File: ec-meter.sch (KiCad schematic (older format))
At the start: 24 parts, among them U1 LM324

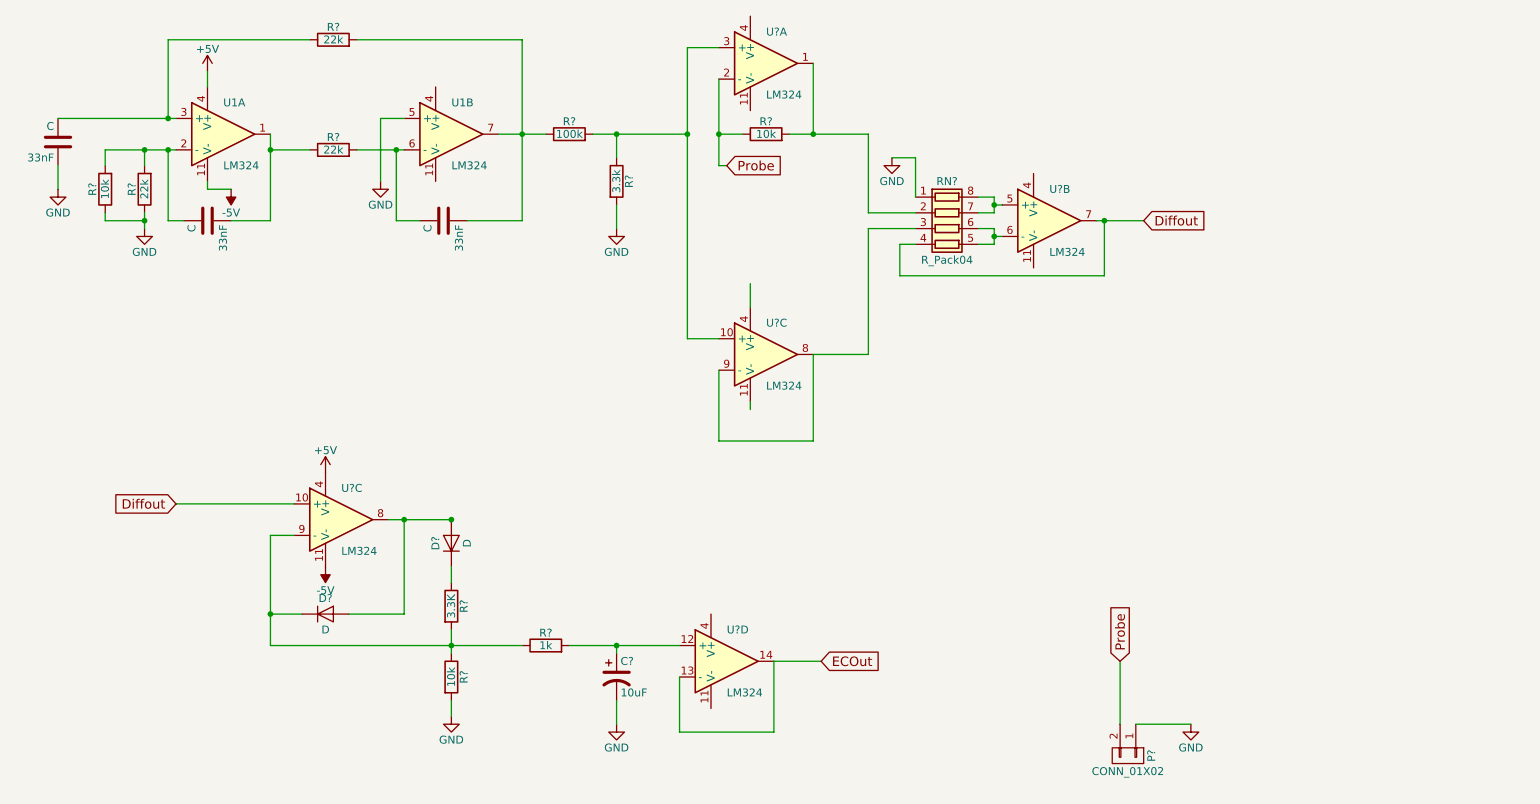
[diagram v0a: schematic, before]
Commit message: Got schematic to pass DRC
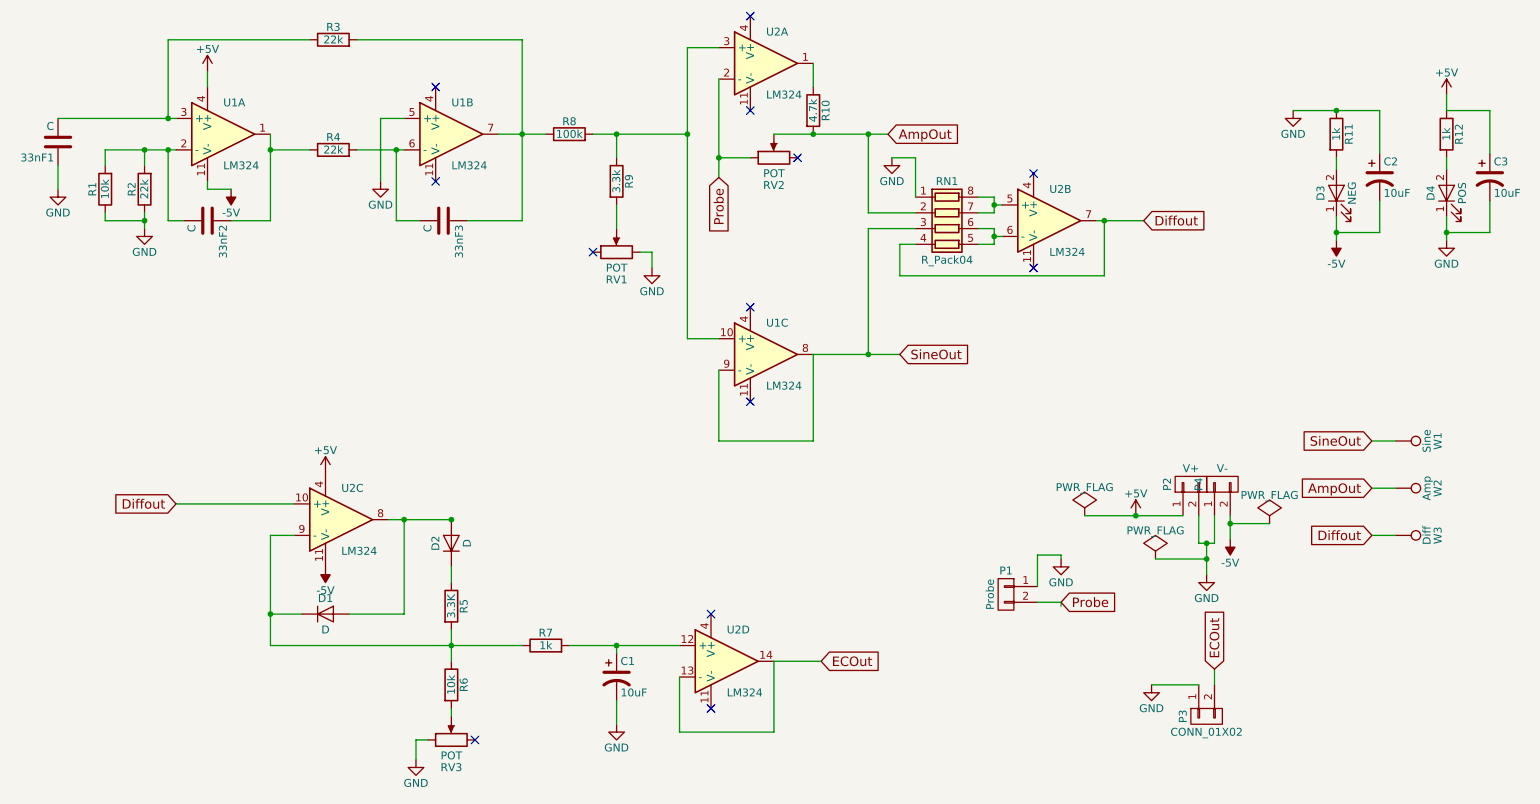
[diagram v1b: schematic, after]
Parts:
- added C2, C3: 10uF, symbol CP1
- added D3: NEG, symbol LED
- added D4: POS, symbol LED
- added P2: V+, symbol CONN_01X02
- added P3: CONN_01X02, symbol CONN_01X02
- added P4: V-, symbol CONN_01X02
- added R11, R12: 1k, symbol R
- added RV1, RV2, RV3: POT, symbol POT
- added W1: Sine, symbol TEST_1P
- added W2: Amp, symbol TEST_1P
- added W3: Diff, symbol TEST_1P
- P1: renamed from P?; value CONN_01X02 -> Probe
- R10: renamed from R?; value 10k -> 4.7k
- gave numbers to parts that had none: 15
- renumbered 33nF to 33nF1, 33nF to 33nF2, 33nF to 33nF3
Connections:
- net +5V: now also C3.1, P2.1 (P1), R12.1
- net -5V: now also C2.2, D3.1 (K), P4.2 (P2)
- net Diffout: now also W3.1
- net ECOut: now also P3.2 (P2)
- net GND: now also C2.1, C3.2, D4.1 (K), P2.2 (P2), P3.1 (P1), P4.1 (P1), R11.1, RV1.3, RV3.1; no longer R6.2, R9.2
- net Probe: now also RV2.1; no longer R10.1
- net AmpOut: now reaches R10.2, RN1.2 (R2.1)
- net AmpOut: now also RV2.2, W2.1; no longer U2.1
- net SineOut: now reaches RN1.3 (R3.1), U1.8, U1.9 (-)
- net SineOut: now also W1.1
- new net: R9.2, RV1.2
- new net: R10.1, U2.1
- new net: R6.2, RV3.2
- new net: D3.2 (A), R11.2
- new net: D4.2 (A), R12.2
- no-connect marks 0 -> 13
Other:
- moved on the sheet: P1, R10, R6

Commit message: Mapped componets, fixed some references
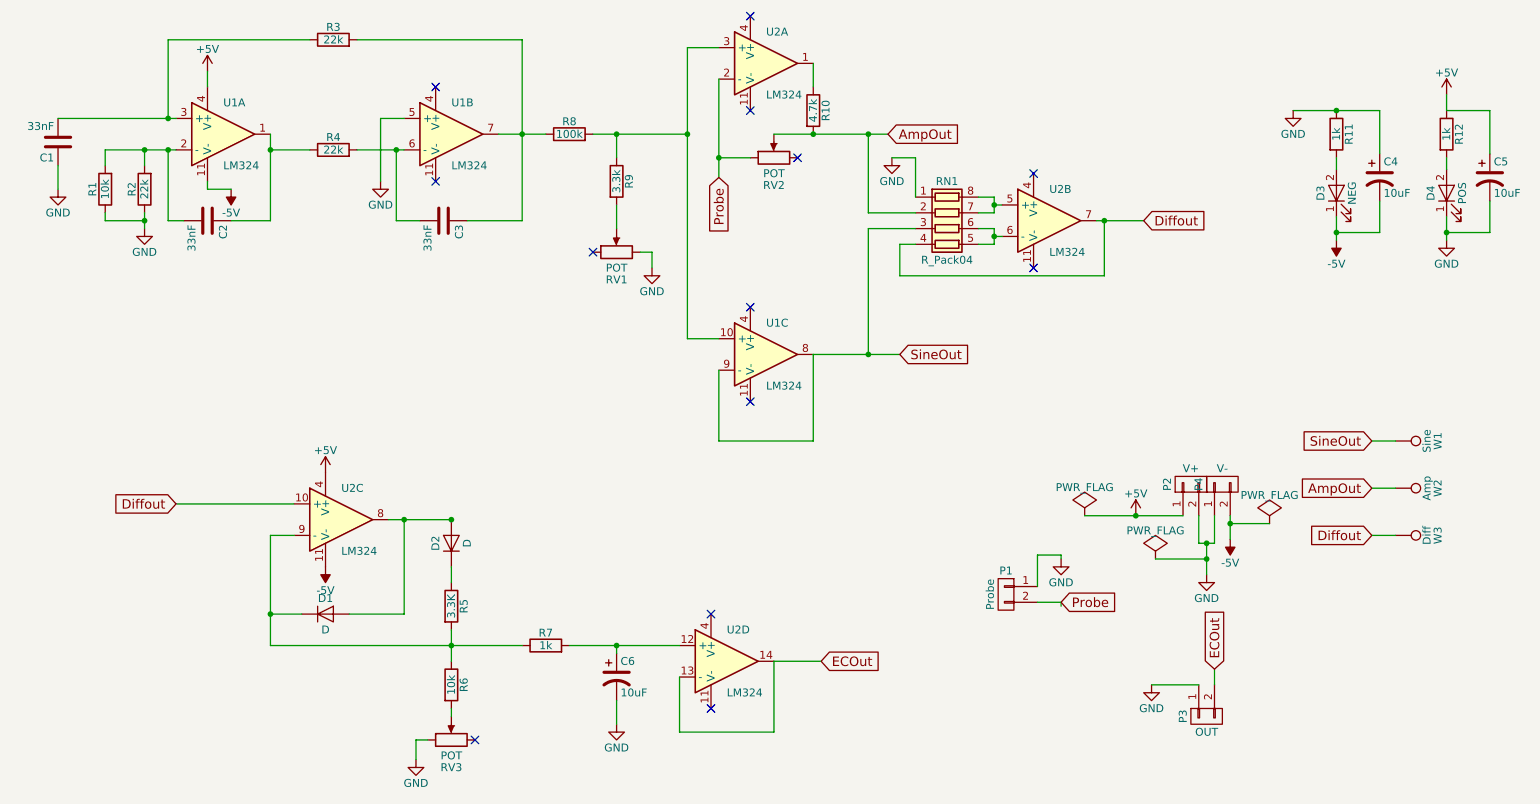
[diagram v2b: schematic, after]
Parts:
- C1: renamed from 33nF1; value C -> 33nF; footprint (none) -> visgence_parts:SM1206POL_VIS
- C2: renamed from 33nF2; value C -> 33nF; footprint (none) -> visgence_parts:SM1206POL_VIS
- C3: renamed from 33nF3; value C -> 33nF; footprint (none) -> visgence_parts:SM1206POL_VIS
- C4: renamed from C2; footprint (none) -> visgence_parts:SM1206POL_VIS
- C6: renamed from C1; footprint (none) -> visgence_parts:SM1206POL_VIS
- P3: value CONN_01X02 -> OUT
- R1, R10, R11, R12, R2, R3, R4, R5, R6, R7, R8, R9: footprint (none) -> visgence_parts:SM1206_VIS
- RN1: footprint (none) -> visgence_parts:RESARRAY-0612
- RV1, RV2, RV3: footprint (none) -> visgence_parts:Var_resistor
- U1, U2: footprint (none) -> SMD_Packages:SOIC-14_N
- W1, W2, W3: footprint (none) -> Measurement_Points:Measurement_Point_Square-TH_Small
- renumbered C3 to C5
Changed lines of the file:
@@
 F 0 "U1" H 2100 2050 50  0000 L CNN
 F 1 "LM324" H 2100 1650 50  0000 L CNN
-F 2 "" H 2050 1950 50  0000 C CNN
+F 2 "SMD_Packages:SOIC-14_N" H 2050 1950 50  0001 C CNN
 F 3 "" H 2150 2050 50  0000 C CNN
 	1    2100 1850
@@
 F 0 "U1" H 3550 2050 50  0000 L CNN
 F 1 "LM324" H 3550 1650 50  0000 L CNN
-F 2 "" H 3500 1950 50  0000 C CNN
+F 2 "SMD_Packages:SOIC-14_N" H 3500 1950 50  0001 C CNN
 F 3 "" H 3600 2050 50  0000 C CNN
 	2    3550 1850
@@
 F 0 "R4" V 2880 1950 50  0000 C CNN
 F 1 "22k" V 2800 1950 50  0000 C CNN
-F 2 "" V 2730 1950 50  0000 C CNN
+F 2 "visgence_parts:SM1206_VIS" V 2730 1950 50  0001 C CNN
 F 3 "" H 2800 1950 50  0000 C CNN
 	1    2800 1950
@@
 F 0 "R2" V 1680 2200 50  0000 C CNN
 F 1 "22k" V 1600 2200 50  0000 C CNN
-F 2 "" V 1530 2200 50  0000 C CNN
+F 2 "visgence_parts:SM1206_VIS" V 1530 2200 50  0001 C CNN
 F 3 "" H 1600 2200 50  0000 C CNN
 	1    1600 2200
@@
 F 0 "R1" V 1430 2200 50  0000 C CNN
 F 1 "10k" V 1350 2200 50  0000 C CNN
-F 2 "" V 1280 2200 50  0000 C CNN
+F 2 "visgence_parts:SM1206_VIS" V 1280 2200 50  0001 C CNN
 F 3 "" H 1350 2200 50  0000 C CNN
 	1    1350 2200
@@
 Connection ~ 1600 2400
 $Comp
-L C 33nF2
+L C C2
 U 1 1 58825F83
 P 2000 2400
-F 0 "33nF2" H 2025 2500 50  0000 L CNN
-F 1 "C" H 2025 2300 50  0000 L CNN
-F 2 "" H 2038 2250 50  0000 C CNN
+F 0 "C2" H 2025 2500 50  0000 L CNN
+F 1 "33nF" H 2025 2300 50  0000 L CNN
+F 2 "visgence_parts:SM1206POL_VIS" H 2038 2250 50  0001 C CNN
 F 3 "" H 2000 2400 50  0000 C CNN
 	1    2000 2400
@@
 Connection ~ 1750 1950
 $Comp
-L C 33nF1
+L C C1
 U 1 1 5882608A
 P 1050 1900
-F 0 "33nF1" H 1075 2000 50  0000 L CNN
-F 1 "C" H 1075 1800 50  0000 L CNN
-F 2 "" H 1088 1750 50  0000 C CNN
+F 0 "C1" H 1075 2000 50  0000 L CNN
+F 1 "33nF" H 1075 1800 50  0000 L CNN
+F 2 "visgence_parts:SM1206POL_VIS" H 1088 1750 50  0001 C CNN
 F 3 "" H 1050 1900 50  0000 C CNN
 	1    1050 1900
@@
 F 0 "R3" V 2880 1250 50  0000 C CNN
 F 1 "22k" V 2800 1250 50  0000 C CNN
-F 2 "" V 2730 1250 50  0000 C CNN
+F 2 "visgence_parts:SM1206_VIS" V 2730 1250 50  0001 C CNN
 F 3 "" H 2800 1250 50  0000 C CNN
 	1    2800 1250
@@
 	4000 2400 4000 1250
 $Comp
-L C 33nF3
+L C C3
 U 1 1 58826293
 P 3500 2400
-F 0 "33nF3" H 3525 2500 50  0000 L CNN
-F 1 "C" H 3525 2300 50  0000 L CNN
-F 2 "" H 3538 2250 50  0000 C CNN
+F 0 "C3" H 3525 2500 50  0000 L CNN
+F 1 "33nF" H 3525 2300 50  0000 L CNN
+F 2 "visgence_parts:SM1206POL_VIS" H 3538 2250 50  0001 C CNN
 F 3 "" H 3500 2400 50  0000 C CNN
 	1    3500 2400
@@
 F 0 "R8" V 4380 1850 50  0000 C CNN
 F 1 "100k" V 4300 1850 50  0000 C CNN
-F 2 "" V 4230 1850 50  0000 C CNN
+F 2 "visgence_parts:SM1206_VIS" V 4230 1850 50  0001 C CNN
 F 3 "" H 4300 1850 50  0000 C CNN
 	1    4300 1850
@@
 F 0 "R9" V 4680 2150 50  0000 C CNN
 F 1 "3.3k" V 4600 2150 50  0000 C CNN
-F 2 "" V 4530 2150 50  0000 C CNN
+F 2 "visgence_parts:SM1206_VIS" V 4530 2150 50  0001 C CNN
 F 3 "" H 4600 2150 50  0000 C CNN
 	1    4600 2150
@@
 F 0 "U2" H 5550 1600 50  0000 L CNN
 F 1 "LM324" H 5550 1200 50  0000 L CNN
-F 2 "" H 5500 1500 50  0000 C CNN
+F 2 "SMD_Packages:SOIC-14_N" H 5500 1500 50  0001 C CNN
 F 3 "" H 5600 1600 50  0000 C CNN
 	1    5550 1400
@@
 F 0 "U2" H 7350 2600 50  0000 L CNN
 F 1 "LM324" H 7350 2200 50  0000 L CNN
-F 2 "" H 7300 2500 50  0000 C CNN
+F 2 "SMD_Packages:SOIC-14_N" H 7300 2500 50  0001 C CNN
 F 3 "" H 7400 2600 50  0000 C CNN
 	2    7350 2400
@@
 F 0 "U2" H 2850 4500 50  0000 L CNN
 F 1 "LM324" H 2850 4100 50  0000 L CNN
-F 2 "" H 2800 4400 50  0000 C CNN
+F 2 "SMD_Packages:SOIC-14_N" H 2800 4400 50  0001 C CNN
 F 3 "" H 2900 4500 50  0000 C CNN
 	3    2850 4300
@@
 F 0 "U2" H 5300 5400 50  0000 L CNN
 F 1 "LM324" H 5300 5000 50  0000 L CNN
-F 2 "" H 5250 5300 50  0000 C CNN
+F 2 "SMD_Packages:SOIC-14_N" H 5250 5300 50  0001 C CNN
 F 3 "" H 5350 5400 50  0000 C CNN
 	4    5300 5200
@@
 F 0 "R10" V 5930 1700 50  0000 C CNN
 F 1 "4.7k" V 5850 1700 50  0000 C CNN
-F 2 "" V 5780 1700 50  0000 C CNN
+F 2 "visgence_parts:SM1206_VIS" V 5780 1700 50  0001 C CNN
 F 3 "" H 5850 1700 50  0000 C CNN
 	1    5850 1700
@@
 F 0 "P1" H 7075 4925 50  0000 C CNN
 F 1 "Probe" V 7175 4775 50  0000 C CNN
-F 2 "" H 7075 4775 50  0000 C CNN
+F 2 "" H 7075 4775 50  0001 C CNN
 F 3 "" H 7075 4775 50  0000 C CNN
 	1    7075 4775
@@
 F 0 "RN1" V 6400 2450 50  0000 C CNN
 F 1 "R_Pack04" V 6900 2450 50  0000 C CNN
-F 2 "" V 6975 2450 50  0001 C CNN
+F 2 "visgence_parts:RESARRAY-0612" V 6975 2450 50  0001 C CNN
 F 3 "" H 6700 2450 50  0000 C CNN
 	1    6700 2450
@@
 F 0 "D1" H 2750 5000 50  0000 C CNN
 F 1 "D" H 2750 4800 50  0000 C CNN
-F 2 "" H 2750 4900 50  0000 C CNN
+F 2 "" H 2750 4900 50  0001 C CNN
 F 3 "" H 2750 4900 50  0000 C CNN
 	1    2750 4900
@@
 F 0 "D2" H 3550 4550 50  0000 C CNN
 F 1 "D" H 3550 4350 50  0000 C CNN
-F 2 "" H 3550 4450 50  0000 C CNN
+F 2 "" H 3550 4450 50  0001 C CNN
 F 3 "" H 3550 4450 50  0000 C CNN
 	1    3550 4450
@@
 F 0 "R5" V 3630 4850 50  0000 C CNN
 F 1 "3.3K" V 3550 4850 50  0000 C CNN
-F 2 "" V 3480 4850 50  0000 C CNN
+F 2 "visgence_parts:SM1206_VIS" V 3480 4850 50  0001 C CNN
 F 3 "" H 3550 4850 50  0000 C CNN
 	1    3550 4850
@@
 F 0 "R7" V 4230 5100 50  0000 C CNN
 F 1 "1k" V 4150 5100 50  0000 C CNN
-F 2 "" V 4080 5100 50  0000 C CNN
+F 2 "visgence_parts:SM1206_VIS" V 4080 5100 50  0001 C CNN
 F 3 "" H 4150 5100 50  0000 C CNN
 	1    4150 5100
@@
 Connection ~ 3550 5100
 $Comp
-L CP1 C1
+L CP1 C6
 U 1 1 5882F85D
 P 4600 5300
-F 0 "C1" H 4625 5400 50  0000 L CNN
+F 0 "C6" H 4625 5400 50  0000 L CNN
 F 1 "10uF" H 4625 5200 50  0000 L CNN
-F 2 "" H 4600 5300 50  0000 C CNN
+F 2 "visgence_parts:SM1206POL_VIS" H 4600 5300 50  0001 C CNN
 F 3 "" H 4600 5300 50  0000 C CNN
 	1    4600 5300
@@
 F 0 "U1" H 5550 3450 50  0000 L CNN
 F 1 "LM324" H 5550 3050 50  0000 L CNN
-F 2 "" H 5500 3350 50  0000 C CNN
+F 2 "SMD_Packages:SOIC-14_N" H 5500 3350 50  0001 C CNN
 F 3 "" H 5600 3450 50  0000 C CNN
 	3    5550 3250
@@
 F 0 "P2" H 8250 4225 50  0000 C CNN
 F 1 "V+" V 8350 4075 50  0000 C CNN
-F 2 "" H 8250 4075 50  0000 C CNN
+F 2 "" H 8250 4075 50  0001 C CNN
 F 3 "" H 8250 4075 50  0000 C CNN
 	1    8250 4075
@@
 F 0 "P4" H 8450 4225 50  0000 C CNN
 F 1 "V-" V 8550 4075 50  0000 C CNN
-F 2 "" H 8450 4075 50  0000 C CNN
+F 2 "" H 8450 4075 50  0001 C CNN
 F 3 "" H 8450 4075 50  0000 C CNN
 	1    8450 4075
@@
 P 8350 5550
 F 0 "P3" H 8350 5700 50  0000 C CNN
-F 1 "CONN_01X02" V 8450 5550 50  0000 C CNN
-F 2 "" H 8350 5550 50  0000 C CNN
+F 1 "OUT" V 8450 5550 50  0000 C CNN
+F 2 "" H 8350 5550 50  0001 C CNN
 F 3 "" H 8350 5550 50  0000 C CNN
 	1    8350 5550
@@
 F 0 "RV2" V 5425 2000 50  0000 C CNN
 F 1 "POT" V 5500 2000 50  0000 C CNN
-F 2 "" H 5600 2000 50  0000 C CNN
+F 2 "visgence_parts:Var_resistor" H 5600 2000 50  0001 C CNN
 F 3 "" H 5600 2000 50  0000 C CNN
 	1    5600 2000
@@
 F 0 "RV3" V 3375 5700 50  0000 C CNN
 F 1 "POT" V 3450 5700 50  0000 C CNN
-F 2 "" H 3550 5700 50  0000 C CNN
+F 2 "visgence_parts:Var_resistor" H 3550 5700 50  0001 C CNN
 F 3 "" H 3550 5700 50  0000 C CNN
 	1    3550 5700
@@
 F 0 "R6" V 3630 5350 50  0000 C CNN
 F 1 "10k" V 3550 5350 50  0000 C CNN
-F 2 "" V 3480 5350 50  0000 C CNN
+F 2 "visgence_parts:SM1206_VIS" V 3480 5350 50  0001 C CNN
 F 3 "" H 3550 5350 50  0000 C CNN
 	1    3550 5350
@@
 F 0 "RV1" V 4425 2600 50  0000 C CNN
 F 1 "POT" V 4500 2600 50  0000 C CNN
-F 2 "" H 4600 2600 50  0000 C CNN
+F 2 "visgence_parts:Var_resistor" H 4600 2600 50  0001 C CNN
 F 3 "" H 4600 2600 50  0000 C CNN
 	1    4600 2600
@@
 F 0 "R11" V 9255 1850 50  0000 C CNN
 F 1 "1k" V 9175 1850 50  0000 C CNN
-F 2 "" V 9105 1850 50  0000 C CNN
+F 2 "visgence_parts:SM1206_VIS" V 9105 1850 50  0001 C CNN
 F 3 "" H 9175 1850 50  0000 C CNN
 	1    9175 1850
@@
 F 0 "D3" H 9175 2325 50  0000 C CNN
 F 1 "NEG" H 9175 2125 50  0000 C CNN
-F 2 "" H 9175 2225 50  0000 C CNN
+F 2 "" H 9175 2225 50  0001 C CNN
 F 3 "" H 9175 2225 50  0000 C CNN
 	1    9175 2225
@@
 Connection ~ 9175 2475
 $Comp
-L CP1 C2
+L CP1 C4
 U 1 1 5886CB8B
 P 9450 2125
-F 0 "C2" H 9475 2225 50  0000 L CNN
+F 0 "C4" H 9475 2225 50  0000 L CNN
 F 1 "10uF" H 9475 2025 50  0000 L CNN
-F 2 "" H 9450 2125 50  0000 C CNN
+F 2 "visgence_parts:SM1206POL_VIS" H 9450 2125 50  0001 C CNN
 F 3 "" H 9450 2125 50  0000 C CNN
 	1    9450 2125
@@
 F 0 "R12" V 9955 1850 50  0000 C CNN
 F 1 "1k" V 9875 1850 50  0000 C CNN
-F 2 "" V 9805 1850 50  0000 C CNN
+F 2 "visgence_parts:SM1206_VIS" V 9805 1850 50  0001 C CNN
 F 3 "" H 9875 1850 50  0000 C CNN
 	1    9875 1850
@@
 F 0 "D4" H 9875 2325 50  0000 C CNN
 F 1 "POS" H 9875 2125 50  0000 C CNN
-F 2 "" H 9875 2225 50  0000 C CNN
+F 2 "" H 9875 2225 50  0001 C CNN
 F 3 "" H 9875 2225 50  0000 C CNN
 	1    9875 2225
@@
 Connection ~ 9875 2475
 $Comp
-L CP1 C3
+L CP1 C5
 U 1 1 5886D1CB
 P 10150 2125
-F 0 "C3" H 10175 2225 50  0000 L CNN
+F 0 "C5" H 10175 2225 50  0000 L CNN
 F 1 "10uF" H 10175 2025 50  0000 L CNN
-F 2 "" H 10150 2125 50  0000 C CNN
+F 2 "" H 10150 2125 50  0001 C CNN
 F 3 "" H 10150 2125 50  0000 C CNN
 	1    10150 2125
@@
 F 0 "W1" H 9550 4070 50  0000 C CNN
 F 1 "Sine" H 9550 4000 50  0000 C CNN
-F 2 "" H 9750 3800 50  0000 C CNN
+F 2 "Measurement_Points:Measurement_Point_Square-TH_Small" H 9750 3800 50  0001 C CNN
 F 3 "" H 9750 3800 50  0000 C CNN
 	1    9550 3800
@@
 F 0 "W2" H 9550 4370 50  0000 C CNN
 F 1 "Amp" H 9550 4300 50  0000 C CNN
-F 2 "" H 9750 4100 50  0000 C CNN
+F 2 "Measurement_Points:Measurement_Point_Square-TH_Small" H 9750 4100 50  0001 C CNN
 F 3 "" H 9750 4100 50  0000 C CNN
 	1    9550 4100
@@
 F 0 "W3" H 9550 4670 50  0000 C CNN
 F 1 "Diff" H 9550 4600 50  0000 C CNN
-F 2 "" H 9750 4400 50  0000 C CNN
+F 2 "Measurement_Points:Measurement_Point_Square-TH_Small" H 9750 4400 50  0001 C CNN
 F 3 "" H 9750 4400 50  0000 C CNN
 	1    9550 4400
